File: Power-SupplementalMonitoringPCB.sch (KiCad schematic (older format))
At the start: 21 parts, among them J1 SWD, SW1 Reset, U1 STM32F413RHTx, Y1 8M

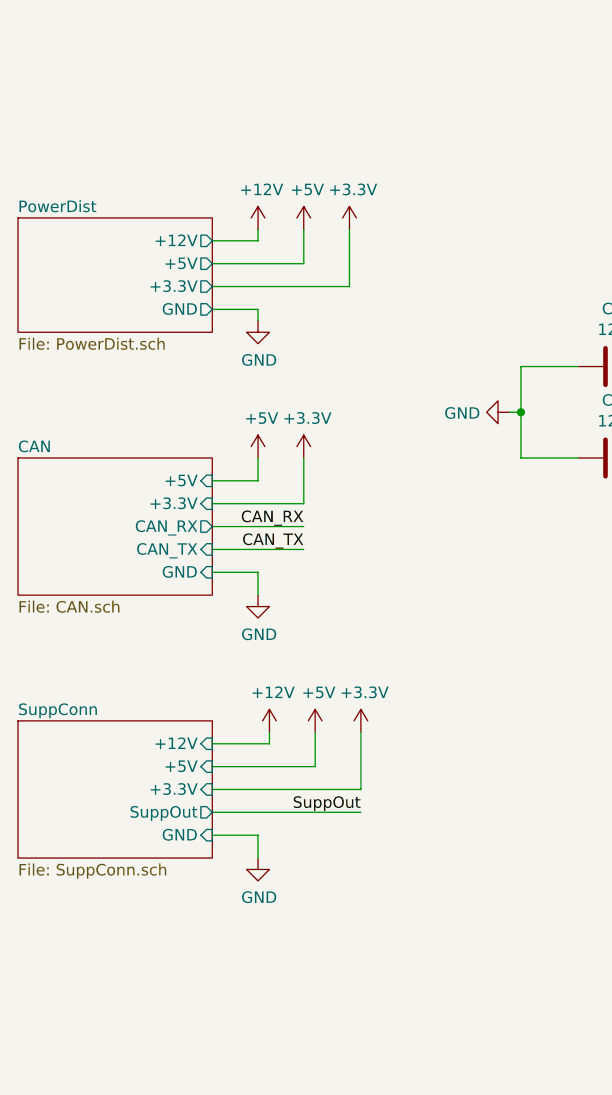
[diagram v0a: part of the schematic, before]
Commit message: Makes edits from critical design review
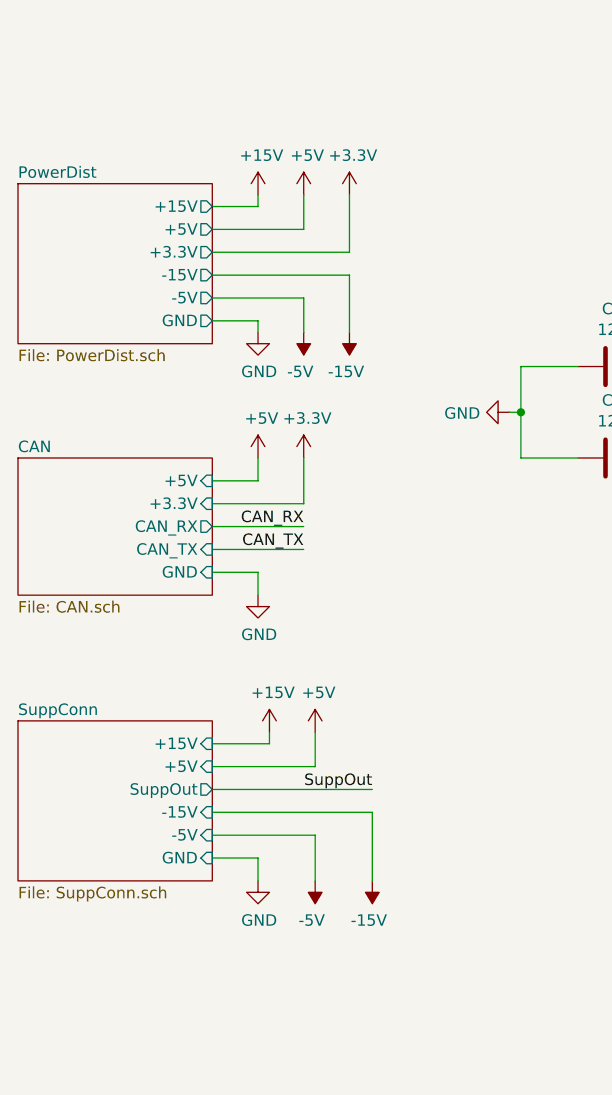
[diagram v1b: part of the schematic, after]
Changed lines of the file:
@@
 CAN_TX
 $Sheet
-S 1550 2650 850  500
+S 1550 2500 850  700
 U 5FD5D696
 F0 "PowerDist" 50
 F1 "PowerDist.sch" 50
-F2 "GND" O R 2400 3050 50
-F3 "+5V" O R 2400 2850 50
-F4 "+3.3V" O R 2400 2950 50
-F5 "+12V" O R 2400 2750 50
+F2 "GND" O R 2400 3100 50
+F3 "+5V" O R 2400 2700 50
+F4 "+3.3V" O R 2400 2800 50
+F5 "-5V" O R 2400 3000 50
+F6 "-15V" O R 2400 2900 50
+F7 "+15V" O R 2400 2600 50
 $EndSheet
 Wire Wire Line
-	2800 2850 2800 2700
+	2800 2700 2800 2550
 $Comp
 L power:+5V #PWR01
 U 1 1 5FD60689
-P 2800 2700
-F 0 "#PWR01" H 2800 2550 50  0001 C CNN
-F 1 "+5V" H 2815 2873 50  0000 C CNN
-F 2 "" H 2800 2700 50  0001 C CNN
-F 3 "" H 2800 2700 50  0001 C CNN
-	1    2800 2700
+P 2800 2550
+F 0 "#PWR01" H 2800 2400 50  0001 C CNN
+F 1 "+5V" H 2815 2723 50  0000 C CNN
+F 2 "" H 2800 2550 50  0001 C CNN
+F 3 "" H 2800 2550 50  0001 C CNN
+	1    2800 2550
 	1    0    0    -1
 $EndComp
@@
 L power:+3.3V #PWR07
 U 1 1 5FD6068F
-P 3000 2700
-F 0 "#PWR07" H 3000 2550 50  0001 C CNN
-F 1 "+3.3V" H 3015 2873 50  0000 C CNN
-F 2 "" H 3000 2700 50  0001 C CNN
-F 3 "" H 3000 2700 50  0001 C CNN
-	1    3000 2700
-	1    0    0    -1
-$EndComp
-Wire Wire Line
-	3000 2700 3000 2950
-Wire Wire Line
-	2600 3050 2600 3100
+P 3000 2550
+F 0 "#PWR07" H 3000 2400 50  0001 C CNN
+F 1 "+3.3V" H 3015 2723 50  0000 C CNN
+F 2 "" H 3000 2550 50  0001 C CNN
+F 3 "" H 3000 2550 50  0001 C CNN
+	1    3000 2550
+	1    0    0    -1
+$EndComp
+Wire Wire Line
+	2600 3100 2600 3150
 $Comp
 L power:GND #PWR02
 U 1 1 5FD633FD
-P 2600 3100
-F 0 "#PWR02" H 2600 2850 50  0001 C CNN
-F 1 "GND" H 2605 2927 50  0000 C CNN
-F 2 "" H 2600 3100 50  0001 C CNN
-F 3 "" H 2600 3100 50  0001 C CNN
-	1    2600 3100
+P 2600 3150
+F 0 "#PWR02" H 2600 2900 50  0001 C CNN
+F 1 "GND" H 2605 2977 50  0000 C CNN
+F 2 "" H 2600 3150 50  0001 C CNN
+F 3 "" H 2600 3150 50  0001 C CNN
+	1    2600 3150
 	1    0    0    -1
 $EndComp
 $Sheet
-S 1550 4850 850  600
+S 1550 4850 850  700
 U 5FD73B7C
 F0 "SuppConn" 50
 F1 "SuppConn.sch" 50
-F2 "SuppOut" O R 2400 5250 50
+F2 "SuppOut" O R 2400 5150 50
 F3 "+5V" I R 2400 5050 50
-F4 "GND" I R 2400 5350 50
-F5 "+3.3V" I R 2400 5150 50
-F6 "+12V" I R 2400 4950 50
+F4 "GND" I R 2400 5450 50
+F5 "+15V" I R 2400 4950 50
+F6 "-5V" I R 2400 5350 50
+F7 "-15V" I R 2400 5250 50
 $EndSheet
 Wire Wire Line
@@
 	1    0    0    -1
 $EndComp
-Text Label 3050 5250 2    50   ~ 0
+Text Label 3100 5150 2    50   ~ 0
 SuppOut
-Wire Wire Line
-	3050 4900 3050 5150
-$Comp
-L power:+3.3V #PWR09
-U 1 1 5FD99E6E
-P 3050 4900
-F 0 "#PWR09" H 3050 4750 50  0001 C CNN
-F 1 "+3.3V" H 3065 5073 50  0000 C CNN
-F 2 "" H 3050 4900 50  0001 C CNN
-F 3 "" H 3050 4900 50  0001 C CNN
-	1    3050 4900
-	1    0    0    -1
-$EndComp
 $Comp
 L power:+5V #PWR05
@@
 Wire Wire Line
 	2850 5050 2850 4900
-$Comp
-L power:+12V #PWR045
-U 1 1 5FF80F3A
-P 2600 2700
-F 0 "#PWR045" H 2600 2550 50  0001 C CNN
-F 1 "+12V" H 2615 2873 50  0000 C CNN
-F 2 "" H 2600 2700 50  0001 C CNN
-F 3 "" H 2600 2700 50  0001 C CNN
-	1    2600 2700
-	1    0    0    -1
-$EndComp
-Wire Wire Line
-	2400 2850 2800 2850
-Wire Wire Line
-	2400 2950 3000 2950
-Wire Wire Line
-	2400 3050 2600 3050
-Wire Wire Line
-	2600 2700 2600 2750
-Wire Wire Line
-	2600 2750 2400 2750
-$Comp
-L power:+12V #PWR046
-U 1 1 5FFB6601
+Wire Wire Line
+	2400 2700 2800 2700
+Wire Wire Line
+	2400 2900 3000 2900
+Wire Wire Line
+	2400 3100 2600 3100
+Wire Wire Line
+	2650 4900 2650 4950
+Wire Wire Line
+	2650 4950 2400 4950
+Wire Wire Line
+	2400 5050 2850 5050
+Wire Wire Line
+	2400 5150 3100 5150
+Wire Wire Line
+	2400 5450 2600 5450
+Wire Wire Line
+	2600 5450 2600 5550
+$Comp
+L power:GND #PWR06
+U 1 1 5FD99E76
+P 2600 5550
+F 0 "#PWR06" H 2600 5300 50  0001 C CNN
+F 1 "GND" H 2605 5377 50  0000 C CNN
+F 2 "" H 2600 5550 50  0001 C CNN
+F 3 "" H 2600 5550 50  0001 C CNN
+	1    2600 5550
+	1    0    0    -1
+$EndComp
+Wire Wire Line
+	2400 3000 2800 3000
+Wire Wire Line
+	2800 3000 2800 3150
+$Comp
+L power:-5V #PWR037
+U 1 1 5FE2AA20
+P 2800 3150
+F 0 "#PWR037" H 2800 3250 50  0001 C CNN
+F 1 "-5V" H 2815 3323 50  0000 C CNN
+F 2 "" H 2800 3150 50  0001 C CNN
+F 3 "" H 2800 3150 50  0001 C CNN
+	1    2800 3150
+	-1   0    0    1
+$EndComp
+$Comp
+L power:+15V #PWR036
+U 1 1 5FE3AC1C
 P 2650 4900
-F 0 "#PWR046" H 2650 4750 50  0001 C CNN
-F 1 "+12V" H 2665 5073 50  0000 C CNN
+F 0 "#PWR036" H 2650 4750 50  0001 C CNN
+F 1 "+15V" H 2665 5073 50  0000 C CNN
 F 2 "" H 2650 4900 50  0001 C CNN
 F 3 "" H 2650 4900 50  0001 C CNN
@@
 $EndComp
 Wire Wire Line
-	2650 4900 2650 4950
-Wire Wire Line
-	2650 4950 2400 4950
-Wire Wire Line
-	2400 5050 2850 5050
-Wire Wire Line
-	2400 5150 3050 5150
-Wire Wire Line
-	2400 5250 3050 5250
-Wire Wire Line
-	2400 5350 2600 5350
-Wire Wire Line
-	2600 5350 2600 5450
-$Comp
-L power:GND #PWR06
-U 1 1 5FD99E76
-P 2600 5450
-F 0 "#PWR06" H 2600 5200 50  0001 C CNN
-F 1 "GND" H 2605 5277 50  0000 C CNN
-F 2 "" H 2600 5450 50  0001 C CNN
-F 3 "" H 2600 5450 50  0001 C CNN
-	1    2600 5450
-	1    0    0    -1
+	2850 5350 2850 5550
+$Comp
+L power:-5V #PWR038
+U 1 1 5FE3B208
+P 2850 5550
+F 0 "#PWR038" H 2850 5650 50  0001 C CNN
+F 1 "-5V" H 2865 5723 50  0000 C CNN
+F 2 "" H 2850 5550 50  0001 C CNN
+F 3 "" H 2850 5550 50  0001 C CNN
+	1    2850 5550
+	-1   0    0    1
+$EndComp
+Wire Wire Line
+	2400 5350 2850 5350
+Wire Wire Line
+	2600 2600 2400 2600
+Wire Wire Line
+	2600 2550 2600 2600
+$Comp
+L power:-15V #PWR?
+U 1 1 5FE33195
+P 3000 3150
+F 0 "#PWR?" H 3000 3250 50  0001 C CNN
+F 1 "-15V" H 3015 3323 50  0000 C CNN
+F 2 "" H 3000 3150 50  0001 C CNN
+F 3 "" H 3000 3150 50  0001 C CNN
+	1    3000 3150
+	-1   0    0    1
+$EndComp
+Wire Wire Line
+	3000 2900 3000 3150
+Wire Wire Line
+	3000 2550 3000 2800
+Wire Wire Line
+	3000 2800 2400 2800
+$Comp
+L power:+15V #PWR?
+U 1 1 5FE472A6
+P 2600 2550
+F 0 "#PWR?" H 2600 2400 50  0001 C CNN
+F 1 "+15V" H 2615 2723 50  0000 C CNN
+F 2 "" H 2600 2550 50  0001 C CNN
+F 3 "" H 2600 2550 50  0001 C CNN
+	1    2600 2550
+	1    0    0    -1
+$EndComp
+Wire Wire Line
+	2400 5250 3100 5250
+Wire Wire Line
+	3100 5250 3100 5550
+$Comp
+L power:-15V #PWR?
+U 1 1 5FE55EAB
+P 3100 5550
+F 0 "#PWR?" H 3100 5650 50  0001 C CNN
+F 1 "-15V" H 3115 5723 50  0000 C CNN
+F 2 "" H 3100 5550 50  0001 C CNN
+F 3 "" H 3100 5550 50  0001 C CNN
+	1    3100 5550
+	-1   0    0    1
 $EndComp
 $EndSCHEMATC

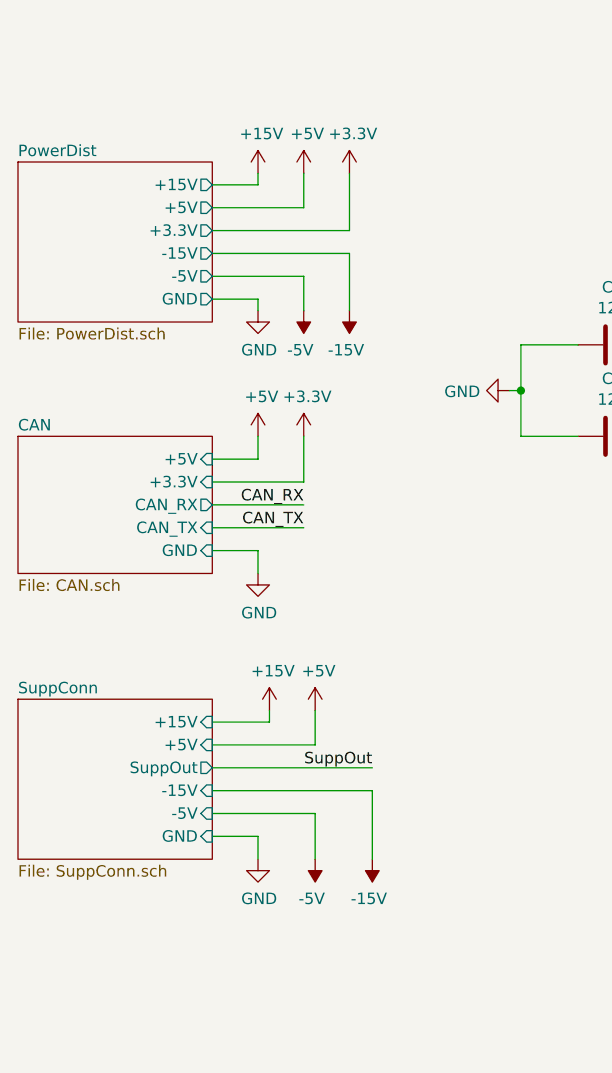
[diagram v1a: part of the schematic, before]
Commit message: Edits opamp circuitry to just one opamp and adds keepout zone under 12V and GNDPWR
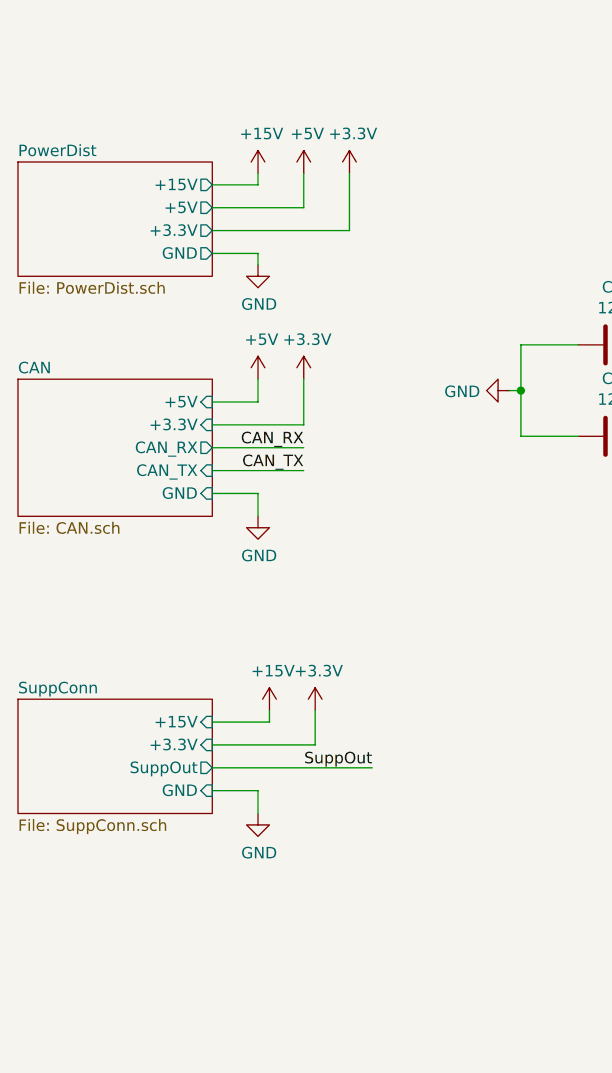
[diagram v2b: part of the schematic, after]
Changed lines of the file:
@@
 Bypass Capacitors
 $Sheet
-S 1550 3700 850  600
+S 1550 3450 850  600
 U 5FD32750
 F0 "CAN" 50
 F1 "CAN.sch" 50
-F2 "+3.3V" I R 2400 3900 50
-F3 "+5V" I R 2400 3800 50
-F4 "GND" I R 2400 4200 50
-F5 "CAN_RX" O R 2400 4000 50
-F6 "CAN_TX" I R 2400 4100 50
+F2 "+3.3V" I R 2400 3650 50
+F3 "+5V" I R 2400 3550 50
+F4 "GND" I R 2400 3950 50
+F5 "CAN_RX" O R 2400 3750 50
+F6 "CAN_TX" I R 2400 3850 50
 $EndSheet
 Wire Wire Line
-	2400 3800 2600 3800
-Wire Wire Line
-	2600 3800 2600 3700
-Wire Wire Line
-	2400 4000 2800 4000
-Wire Wire Line
-	2400 4100 2800 4100
-Wire Wire Line
-	2400 4200 2600 4200
-Wire Wire Line
-	2600 4200 2600 4300
+	2400 3550 2600 3550
+Wire Wire Line
+	2600 3550 2600 3450
+Wire Wire Line
+	2400 3750 2800 3750
+Wire Wire Line
+	2400 3850 2800 3850
+Wire Wire Line
+	2400 3950 2600 3950
+Wire Wire Line
+	2600 3950 2600 4050
 $Comp
 L power:+5V #PWR03
 U 1 1 5FD43B52
-P 2600 3700
-F 0 "#PWR03" H 2600 3550 50  0001 C CNN
-F 1 "+5V" H 2615 3873 50  0000 C CNN
-F 2 "" H 2600 3700 50  0001 C CNN
-F 3 "" H 2600 3700 50  0001 C CNN
-	1    2600 3700
+P 2600 3450
+F 0 "#PWR03" H 2600 3300 50  0001 C CNN
+F 1 "+5V" H 2615 3623 50  0000 C CNN
+F 2 "" H 2600 3450 50  0001 C CNN
+F 3 "" H 2600 3450 50  0001 C CNN
+	1    2600 3450
 	1    0    0    -1
 $EndComp
@@
 L power:+3.3V #PWR08
 U 1 1 5FD43EC5
-P 2800 3700
-F 0 "#PWR08" H 2800 3550 50  0001 C CNN
-F 1 "+3.3V" H 2815 3873 50  0000 C CNN
-F 2 "" H 2800 3700 50  0001 C CNN
-F 3 "" H 2800 3700 50  0001 C CNN
-	1    2800 3700
-	1    0    0    -1
-$EndComp
-Wire Wire Line
-	2800 3700 2800 3900
-Wire Wire Line
-	2400 3900 2800 3900
+P 2800 3450
+F 0 "#PWR08" H 2800 3300 50  0001 C CNN
+F 1 "+3.3V" H 2815 3623 50  0000 C CNN
+F 2 "" H 2800 3450 50  0001 C CNN
+F 3 "" H 2800 3450 50  0001 C CNN
+	1    2800 3450
+	1    0    0    -1
+$EndComp
+Wire Wire Line
+	2800 3450 2800 3650
+Wire Wire Line
+	2400 3650 2800 3650
 $Comp
 L power:GND #PWR04
 U 1 1 5FD5CE76
-P 2600 4300
-F 0 "#PWR04" H 2600 4050 50  0001 C CNN
-F 1 "GND" H 2605 4127 50  0000 C CNN
-F 2 "" H 2600 4300 50  0001 C CNN
-F 3 "" H 2600 4300 50  0001 C CNN
-	1    2600 4300
-	1    0    0    -1
-$EndComp
-Text Label 2800 4000 2    50   ~ 0
+P 2600 4050
+F 0 "#PWR04" H 2600 3800 50  0001 C CNN
+F 1 "GND" H 2605 3877 50  0000 C CNN
+F 2 "" H 2600 4050 50  0001 C CNN
+F 3 "" H 2600 4050 50  0001 C CNN
+	1    2600 4050
+	1    0    0    -1
+$EndComp
+Text Label 2800 3750 2    50   ~ 0
 CAN_RX
-Text Label 2800 4100 2    50   ~ 0
+Text Label 2800 3850 2    50   ~ 0
 CAN_TX
-$Sheet
-S 1550 2500 850  700
-U 5FD5D696
-F0 "PowerDist" 50
-F1 "PowerDist.sch" 50
-F2 "GND" O R 2400 3100 50
-F3 "+5V" O R 2400 2700 50
-F4 "+3.3V" O R 2400 2800 50
-F5 "-5V" O R 2400 3000 50
-F6 "-15V" O R 2400 2900 50
-F7 "+15V" O R 2400 2600 50
-$EndSheet
 Wire Wire Line
 	2800 2700 2800 2550
@@
 $EndComp
 Wire Wire Line
-	2600 3100 2600 3150
+	2600 2900 2600 2950
 $Comp
 L power:GND #PWR02
 U 1 1 5FD633FD
-P 2600 3150
-F 0 "#PWR02" H 2600 2900 50  0001 C CNN
-F 1 "GND" H 2605 2977 50  0000 C CNN
-F 2 "" H 2600 3150 50  0001 C CNN
-F 3 "" H 2600 3150 50  0001 C CNN
-	1    2600 3150
+P 2600 2950
+F 0 "#PWR02" H 2600 2700 50  0001 C CNN
+F 1 "GND" H 2605 2777 50  0000 C CNN
+F 2 "" H 2600 2950 50  0001 C CNN
+F 3 "" H 2600 2950 50  0001 C CNN
+	1    2600 2950
 	1    0    0    -1
 $EndComp
 $Sheet
-S 1550 4850 850  700
+S 1550 4850 850  500
 U 5FD73B7C
 F0 "SuppConn" 50
 F1 "SuppConn.sch" 50
 F2 "SuppOut" O R 2400 5150 50
-F3 "+5V" I R 2400 5050 50
-F4 "GND" I R 2400 5450 50
-F5 "+15V" I R 2400 4950 50
-F6 "-5V" I R 2400 5350 50
-F7 "-15V" I R 2400 5250 50
+F3 "GND" I R 2400 5250 50
+F4 "+15V" I R 2400 4950 50
+F5 "+3.3V" I R 2400 5050 50
 $EndSheet
 Wire Wire Line
@@
 Text Label 3100 5150 2    50   ~ 0
 SuppOut
-$Comp
-L power:+5V #PWR05
-U 1 1 5FD99E68
-P 2850 4900
-F 0 "#PWR05" H 2850 4750 50  0001 C CNN
-F 1 "+5V" H 2865 5073 50  0000 C CNN
-F 2 "" H 2850 4900 50  0001 C CNN
-F 3 "" H 2850 4900 50  0001 C CNN
-	1    2850 4900
-	1    0    0    -1
-$EndComp
 Wire Wire Line
 	2850 5050 2850 4900
@@
 	2400 2700 2800 2700
 Wire Wire Line
-	2400 2900 3000 2900
-Wire Wire Line
-	2400 3100 2600 3100
+	2400 2900 2600 2900
 Wire Wire Line
 	2650 4900 2650 4950
@@
 	2400 5150 3100 5150
 Wire Wire Line
-	2400 5450 2600 5450
-Wire Wire Line
-	2600 5450 2600 5550
+	2400 5250 2600 5250
+Wire Wire Line
+	2600 5250 2600 5350
 $Comp
 L power:GND #PWR06
 U 1 1 5FD99E76
-P 2600 5550
-F 0 "#PWR06" H 2600 5300 50  0001 C CNN
-F 1 "GND" H 2605 5377 50  0000 C CNN
-F 2 "" H 2600 5550 50  0001 C CNN
-F 3 "" H 2600 5550 50  0001 C CNN
-	1    2600 5550
-	1    0    0    -1
-$EndComp
-Wire Wire Line
-	2400 3000 2800 3000
-Wire Wire Line
-	2800 3000 2800 3150
-$Comp
-L power:-5V #PWR037
-U 1 1 5FE2AA20
-P 2800 3150
-F 0 "#PWR037" H 2800 3250 50  0001 C CNN
-F 1 "-5V" H 2815 3323 50  0000 C CNN
-F 2 "" H 2800 3150 50  0001 C CNN
-F 3 "" H 2800 3150 50  0001 C CNN
-	1    2800 3150
-	-1   0    0    1
+P 2600 5350
+F 0 "#PWR06" H 2600 5100 50  0001 C CNN
+F 1 "GND" H 2605 5177 50  0000 C CNN
+F 2 "" H 2600 5350 50  0001 C CNN
+F 3 "" H 2600 5350 50  0001 C CNN
+	1    2600 5350
+	1    0    0    -1
 $EndComp
 $Comp
@@
 $EndComp
 Wire Wire Line
-	2850 5350 2850 5550
-$Comp
-L power:-5V #PWR038
-U 1 1 5FE3B208
-P 2850 5550
-F 0 "#PWR038" H 2850 5650 50  0001 C CNN
-F 1 "-5V" H 2865 5723 50  0000 C CNN
-F 2 "" H 2850 5550 50  0001 C CNN
-F 3 "" H 2850 5550 50  0001 C CNN
-	1    2850 5550
-	-1   0    0    1
-$EndComp
-Wire Wire Line
-	2400 5350 2850 5350
-Wire Wire Line
 	2600 2600 2400 2600
 Wire Wire Line
 	2600 2550 2600 2600
-$Comp
-L power:-15V #PWR?
-U 1 1 5FE33195
-P 3000 3150
-F 0 "#PWR?" H 3000 3250 50  0001 C CNN
-F 1 "-15V" H 3015 3323 50  0000 C CNN
-F 2 "" H 3000 3150 50  0001 C CNN
-F 3 "" H 3000 3150 50  0001 C CNN
-	1    3000 3150
-	-1   0    0    1
-$EndComp
-Wire Wire Line
-	3000 2900 3000 3150
 Wire Wire Line
 	3000 2550 3000 2800
@@
 	3000 2800 2400 2800
 $Comp
-L power:+15V #PWR?
+L power:+15V #PWR0101
 U 1 1 5FE472A6
 P 2600 2550
-F 0 "#PWR?" H 2600 2400 50  0001 C CNN
+F 0 "#PWR0101" H 2600 2400 50  0001 C CNN
 F 1 "+15V" H 2615 2723 50  0000 C CNN
 F 2 "" H 2600 2550 50  0001 C CNN
@@
 	1    0    0    -1
 $EndComp
-Wire Wire Line
-	2400 5250 3100 5250
-Wire Wire Line
-	3100 5250 3100 5550
-$Comp
-L power:-15V #PWR?
-U 1 1 5FE55EAB
-P 3100 5550
-F 0 "#PWR?" H 3100 5650 50  0001 C CNN
-F 1 "-15V" H 3115 5723 50  0000 C CNN
-F 2 "" H 3100 5550 50  0001 C CNN
-F 3 "" H 3100 5550 50  0001 C CNN
-	1    3100 5550
-	-1   0    0    1
+$Sheet
+S 1550 2500 850  500
+U 5FD5D696
+F0 "PowerDist" 50
+F1 "PowerDist.sch" 50
+F2 "GND" O R 2400 2900 50
+F3 "+5V" O R 2400 2700 50
+F4 "+3.3V" O R 2400 2800 50
+F5 "+15V" O R 2400 2600 50
+$EndSheet
+$Comp
+L power:+3.3V #PWR0102
+U 1 1 5FE0C5FB
+P 2850 4900
+F 0 "#PWR0102" H 2850 4750 50  0001 C CNN
+F 1 "+3.3V" H 2865 5073 50  0000 C CNN
+F 2 "" H 2850 4900 50  0001 C CNN
+F 3 "" H 2850 4900 50  0001 C CNN
+	1    2850 4900
+	1    0    0    -1
 $EndComp
 $EndSCHEMATC
